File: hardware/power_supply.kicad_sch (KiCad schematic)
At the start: 24 parts, among them J4 POWER INPUT, U10 NCP1117-5.0, U11 LM2596DS-ADJ, U11 NCP1117-3.3

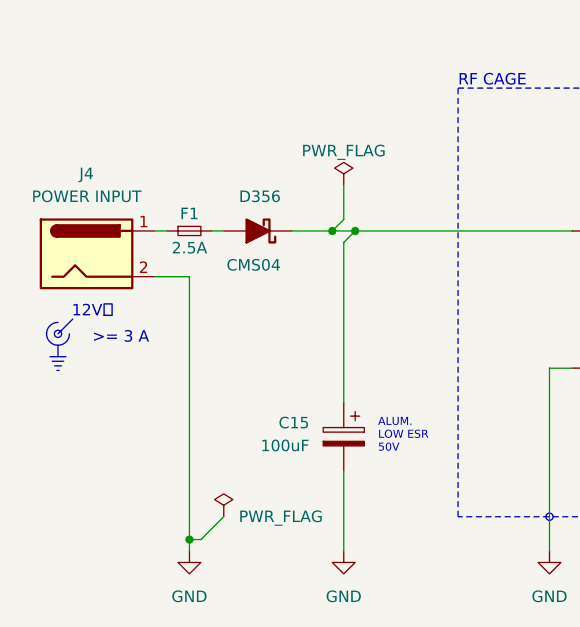
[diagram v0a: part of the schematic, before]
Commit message: Assign footprints
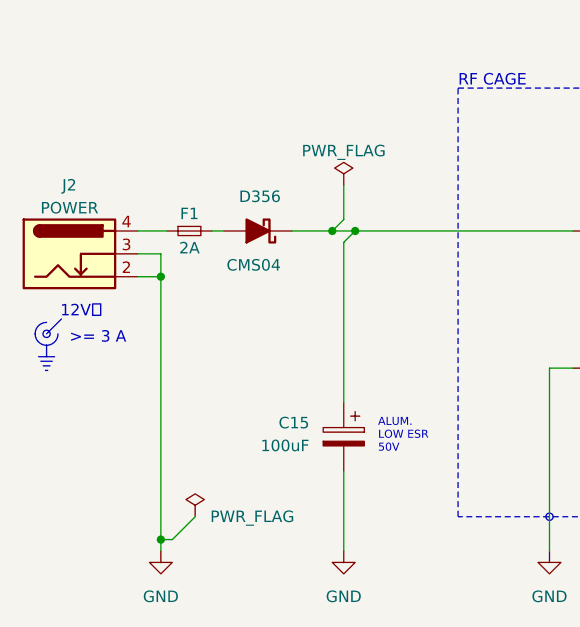
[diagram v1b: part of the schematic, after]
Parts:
- removed J4: POWER INPUT, symbol Connector:Jack-DC
- added J2: POWER, Connector_espena:DC-Power-Jack_DC044_5.5mm_2.1mm, symbol Connector_espena:Barrel_Jack_Switch
- C14, C19, C28: footprint (none) -> Capacitor_SMD_espena:CP_Elec_18x16.5
- C15: footprint (none) -> Capacitor_SMD:CP_Elec_8x10
- C16, C20, C21, C24, C26, C27, C31, C32: footprint (none) -> Capacitor_SMD:C_0805_2012Metric
- D355: footprint (none) -> Diode_SMD:D_SMA
- D356: footprint (none) -> Diode_SMD_mouser:SODFL4724X108N
- F1: value 2.5A -> 2A; footprint (none) -> Fuse_espena:FuseHolder_Keystone_3554
- L1: footprint (none) -> Inductor_SMD_espena:L_Pulse_LCI-44
- R20, R21: footprint (none) -> Resistor_SMD:R_0805_2012Metric
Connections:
- net GND: now also J2.2, J2.3
- net at F1.1: now also J2.4

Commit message: Starting PCB routing process
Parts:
- J2: footprint Connector_espena:DC-Power-Jack_DC044_5.5mm_2.1mm -> Connector_BarrelJack_espena:BarrelJack_DC044_Horizontal
- U11: footprint Package_TO_SOT_THT:TO-220-5_P3.4x3.7mm_StaggerOdd_Lead3.8mm_Vertical -> Regulator_SMD_mouser:NCP5663DSADJR4G
- renumbered U11 to U12, U11 to U13, U11 to U14
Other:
- moved on the sheet: D356, F1, R20, R21

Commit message: Routing in progress
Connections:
- net +3.3V_MCU: now reaches C31.1, U14.2 (VO)
- net +8.1V: now reaches C14.1, C16.2, C21.1, C24.1, C27.1, L1.2, R20.2, U10.3 (VI), U13.3 (VI), U14.3 (VI)
- net +3.3V_LED: now reaches C32.1, U13.2 (VO)
- net +3.3V_GPS: now reaches C26.1, C28.1, U12.2 (VO)
- net +5V: now reaches C19.1, C20.1, U10.2 (VO), U12.3 (VI)
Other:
- note removed: "5.0V"

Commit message: Prototype, starting on firmware
Former-commit-id: 3c22e4f94bda4a4eed472ac1ff762e7709731c05
Former-commit-id: afce4fecf5b4961621dea2f3a514203675ae8e80
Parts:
- added C25: 100uF, Capacitor_SMD:CP_Elec_8x10, symbol Device:C_Polarized
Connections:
- net +8.1V: now also C25.1
- net GND: now also C25.2
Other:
- moved on the sheet: C16, D355, L1, R20, R21, U11

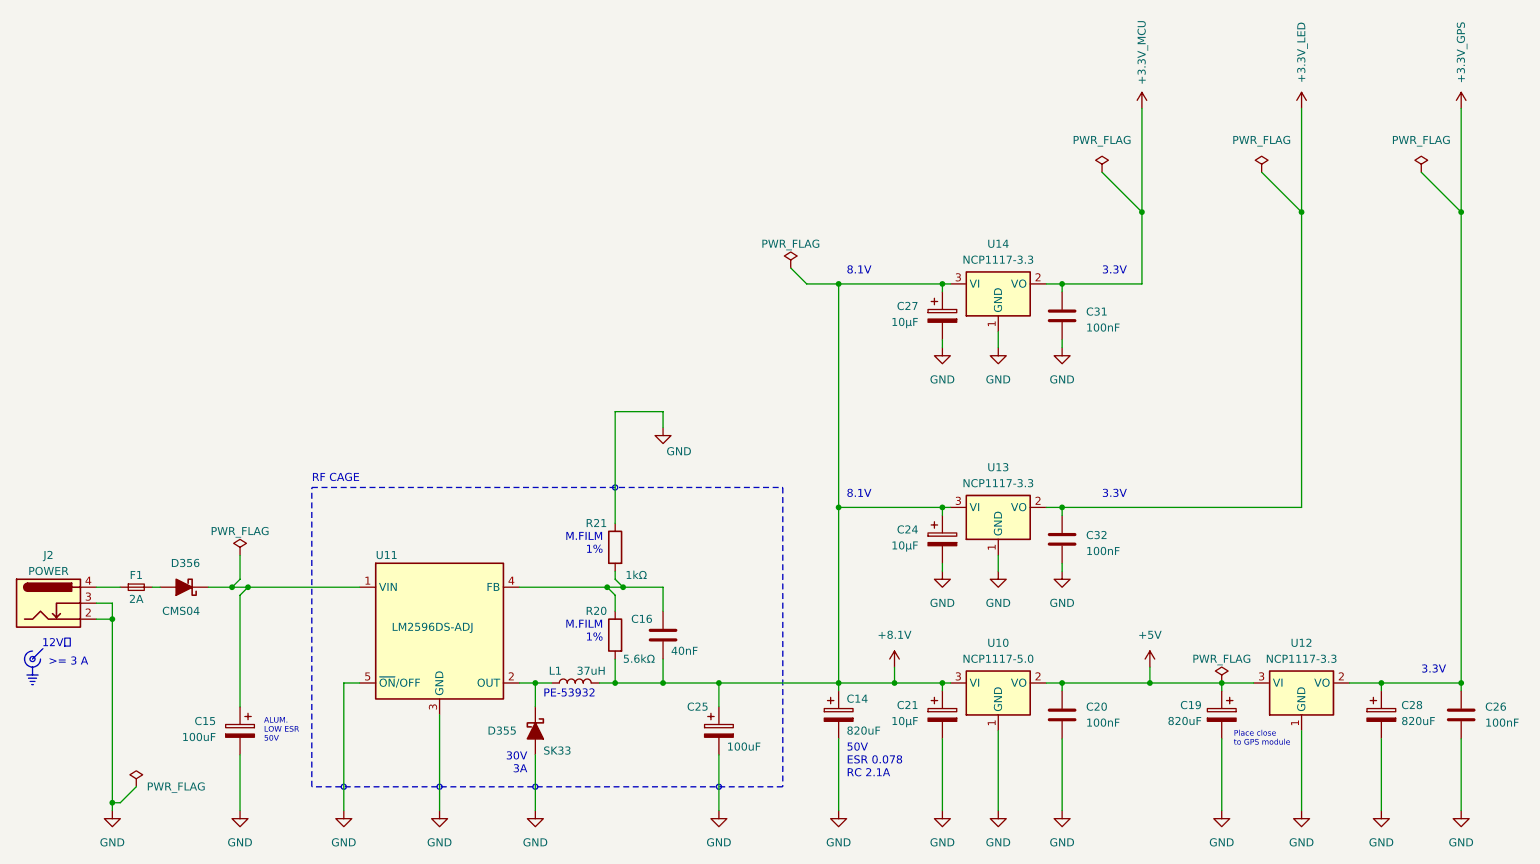
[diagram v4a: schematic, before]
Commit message: Change fuse from 2A to 250 mA
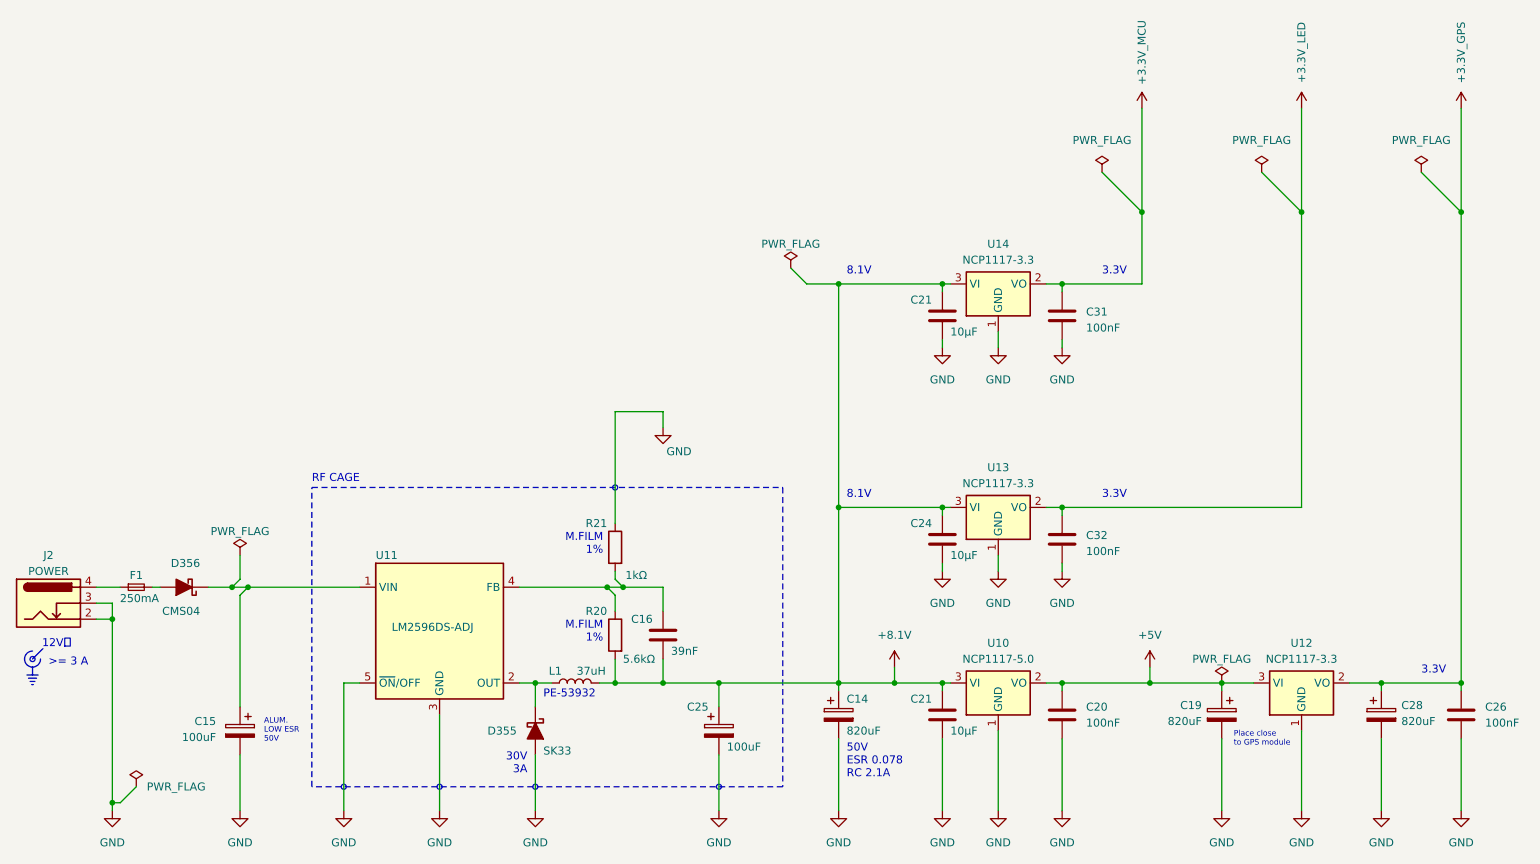
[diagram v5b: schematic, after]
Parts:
- removed C21, C24, C27: 10µF, Capacitor_SMD:C_0805_2012Metric, symbol Device:C_Polarized
- added C21 (x2), C24: 10µF, Capacitor_SMD:C_0805_2012Metric, symbol Device:C
- C16: value 40nF -> 39nF
- F1: value 2A -> 250mA
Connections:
- net +8.1V: now also C21.1, C21.1, C24.1
- net GND: now also C21.2, C21.2, C24.2
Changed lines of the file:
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@@
 	)
 	(symbol
-		(lib_id "Device:C_Polarized")
-		(at 176.53 132.08 0)
-		(unit 1)
-		(exclude_from_sim no)
-		(in_bom yes)
-		(on_board yes)
-		(dnp no)
-		(property "Reference" "C21"
-			(at 172.72 130.556 0)
-			(effects
-				(font
-					(size 1.27 1.27)
-				)
-				(justify right)
-			)
-		)
-		(property "Value" "10µF"
-			(at 172.72 133.096 0)
-			(effects
-				(font
-					(size 1.27 1.27)
-				)
-				(justify right)
-			)
-		)
-		(property "Footprint" "Capacitor_SMD:C_0805_2012Metric"
-			(at 177.4952 135.89 0)
-			(effects
-				(font
-					(size 1.27 1.27)
-				)
-				(hide yes)
-			)
-		)
-		(property "Datasheet" "~"
-			(at 176.53 132.08 0)
-			(effects
-				(font
-					(size 1.27 1.27)
-				)
-				(hide yes)
-			)
-		)
-		(property "Description" "Polarized capacitor"
-			(at 176.53 132.08 0)
-			(effects
-				(font
-					(size 1.27 1.27)
-				)
-				(hide yes)
-			)
-		)
-		(pin "1"
-		)
-		(pin "2"
-		)
-		(instances
-			(project "broadcast_clock"
-				(path "/40ecfd14-7e3d-4342-87f4-c464dfcd4cdf/08d14882-9adb-43c1-98ed-4244eb646c28"
-					(reference "C21")
-					(unit 1)
-				)
-			)
-		)
-	)
-	(symbol
 		(lib_id "Device:L")
 		(at 118.11 127 90)
@@
 	)
 	(symbol
-		(lib_id "Device:C_Polarized")
-		(at 176.53 68.58 0)
-		(unit 1)
-		(exclude_from_sim no)
-		(in_bom yes)
-		(on_board yes)
-		(dnp no)
-		(property "Reference" "C27"
-			(at 172.72 67.056 0)
-			(effects
-				(font
-					(size 1.27 1.27)
-				)
-				(justify right)
-			)
-		)
-		(property "Value" "10µF"
-			(at 172.72 69.596 0)
-			(effects
-				(font
-					(size 1.27 1.27)
-				)
-				(justify right)
-			)
-		)
-		(property "Footprint" "Capacitor_SMD:C_0805_2012Metric"
-			(at 177.4952 72.39 0)
-			(effects
-				(font
-					(size 1.27 1.27)
-				)
-				(hide yes)
-			)
-		)
-		(property "Datasheet" "~"
-			(at 176.53 68.58 0)
-			(effects
-				(font
-					(size 1.27 1.27)
-				)
-				(hide yes)
-			)
-		)
-		(property "Description" "Polarized capacitor"
-			(at 176.53 68.58 0)
-			(effects
-				(font
-					(size 1.27 1.27)
-				)
-				(hide yes)
-			)
-		)
-		(pin "1"
-		)
-		(pin "2"
-		)
-		(instances
-			(project "broadcast_clock"
-				(path "/40ecfd14-7e3d-4342-87f4-c464dfcd4cdf/08d14882-9adb-43c1-98ed-4244eb646c28"
-					(reference "C27")
-					(unit 1)
-				)
-			)
-		)
-	)
-	(symbol
 		(lib_id "power:GND")
 		(at 185.42 73.66 0)
@@
 	)
 	(symbol
+		(lib_id "Device:C")
+		(at 176.53 132.08 0)
+		(unit 1)
+		(exclude_from_sim no)
+		(in_bom yes)
+		(on_board yes)
+		(dnp no)
+		(property "Reference" "C21"
+			(at 171.45 129.54 0)
+			(effects
+				(font
+					(size 1.27 1.27)
+				)
+				(justify left)
+			)
+		)
+		(property "Value" "10µF"
+			(at 177.8 134.62 0)
+			(effects
+				(font
+					(size 1.27 1.27)
+				)
+				(justify left)
+			)
+		)
+		(property "Footprint" "Capacitor_SMD:C_0805_2012Metric"
+			(at 177.4952 135.89 0)
+			(effects
+				(font
+					(size 1.27 1.27)
+				)
+				(hide yes)
+			)
+		)
+		(property "Datasheet" "~"
+			(at 176.53 132.08 0)
+			(effects
+				(font
+					(size 1.27 1.27)
+				)
+				(hide yes)
+			)
+		)
+		(property "Description" "Unpolarized capacitor"
+			(at 176.53 132.08 0)
+			(effects
+				(font
+					(size 1.27 1.27)
+				)
+				(hide yes)
+			)
+		)
+		(pin "1"
+		)
+		(pin "2"
+		)
+		(instances
+			(project "broadcast_clock"
+				(path "/40ecfd14-7e3d-4342-87f4-c464dfcd4cdf/08d14882-9adb-43c1-98ed-4244eb646c28"
+					(reference "C21")
+					(unit 1)
+				)
+			)
+		)
+	)
+	(symbol
 		(lib_id "power_espena:+5V")
 		(at 209.55 124.46 0)
@@
 			)
 		)
-		(property "Value" "40nF"
+		(property "Value" "39nF"
 			(at 133.35 121.92 0)
 			(effects
@@
 			)
 		)
-		(property "Value" "2A"
-			(at 48.26 113.665 0)
+		(property "Value" "250mA"
+			(at 48.768 113.538 0)
 			(effects
 				(font
@@
 	(symbol
 		(lib_id "Device:C_Polarized")
-		(at 176.53 104.14 0)
-		(unit 1)
-		(exclude_from_sim no)
-		(in_bom yes)
-		(on_board yes)
-		(dnp no)
-		(property "Reference" "C24"
-			(at 172.72 102.616 0)
-			(effects
-				(font
-					(size 1.27 1.27)
-				)
-				(justify right)
-			)
-		)
-		(property "Value" "10µF"
-			(at 172.72 105.156 0)
-			(effects
-				(font
-					(size 1.27 1.27)
-				)
-				(justify right)
-			)
-		)
-		(property "Footprint" "Capacitor_SMD:C_0805_2012Metric"
-			(at 177.4952 107.95 0)
-			(effects
-				(font
-					(size 1.27 1.27)
-				)
-				(hide yes)
-			)
-		)
-		(property "Datasheet" "~"
-			(at 176.53 104.14 0)
-			(effects
-				(font
-					(size 1.27 1.27)
-				)
-				(hide yes)
-			)
-		)
-		(property "Description" "Polarized capacitor"
-			(at 176.53 104.14 0)
-			(effects
-				(font
-					(size 1.27 1.27)
-				)
-				(hide yes)
-			)
-		)
-		(pin "1"
-		)
-		(pin "2"
-		)
-		(instances
-			(project "broadcast_clock"
-				(path "/40ecfd14-7e3d-4342-87f4-c464dfcd4cdf/08d14882-9adb-43c1-98ed-4244eb646c28"
-					(reference "C24")
-					(unit 1)
-				)
-			)
-		)
-	)
-	(symbol
-		(lib_id "Device:C_Polarized")
 		(at 220.98 132.08 0)
 		(mirror y)
@@
 					(unit 1)
 				)
+			)
+		)
+	)
+	(symbol
+		(lib_id "Device:C")
+		(at 176.53 104.14 0)
+		(unit 1)
+		(exclude_from_sim no)
+		(in_bom yes)
+		(on_board yes)
+		(dnp no)
+		(property "Reference" "C24"
+			(at 171.45 101.6 0)
+			(effects
+				(font
+					(size 1.27 1.27)
+				)
+				(justify left)
+			)
+		)
+		(property "Value" "10µF"
+			(at 177.8 106.68 0)
+			(effects
+				(font
+					(size 1.27 1.27)
+				)
+				(justify left)
+			)
+		)
+		(property "Footprint" "Capacitor_SMD:C_0805_2012Metric"
+			(at 177.4952 107.95 0)
+			(effects
+				(font
+					(size 1.27 1.27)
+				)
+				(hide yes)
+			)
+		)
+		(property "Datasheet" "~"
+			(at 176.53 104.14 0)
+			(effects
+				(font
+					(size 1.27 1.27)
+				)
+				(hide yes)
+			)
+		)
+		(property "Description" "Unpolarized capacitor"
+			(at 176.53 104.14 0)
+			(effects
+				(font
+					(size 1.27 1.27)
+				)
+				(hide yes)
+			)
+		)
+		(pin "1"
+		)
+		(pin "2"
+		)
+		(instances
+			(project "broadcast_clock"
+				(path "/40ecfd14-7e3d-4342-87f4-c464dfcd4cdf/08d14882-9adb-43c1-98ed-4244eb646c28"
+					(reference "C24")
+					(unit 1)
+				)
+			)
+		)
+	)
+	(symbol
+		(lib_id "Device:C")
+		(at 176.53 68.58 0)
+		(unit 1)
+		(exclude_from_sim no)
+		(in_bom yes)
+		(on_board yes)
+		(dnp no)
+		(property "Reference" "C21"
+			(at 171.45 66.04 0)
+			(effects
+				(font
+					(size 1.27 1.27)
+				)
+				(justify left)
+			)
+		)
+		(property "Value" "10µF"
+			(at 177.8 71.12 0)
+			(effects
+				(font
+					(size 1.27 1.27)
+				)
+				(justify left)
+			)
+		)
+		(property "Footprint" "Capacitor_SMD:C_0805_2012Metric"
+			(at 177.4952 72.39 0)
+			(effects
+				(font
+					(size 1.27 1.27)
+				)
+				(hide yes)
+			)
+		)
+		(property "Datasheet" "~"
+			(at 176.53 68.58 0)
+			(effects
+				(font
+					(size 1.27 1.27)
+				)
+				(hide yes)
+			)
+		)
+		(property "Description" "Unpolarized capacitor"
+			(at 176.53 68.58 0)
+			(effects
+				(font
+					(size 1.27 1.27)
+				)
+				(hide yes)
+			)
+		)
+		(pin "1"
+		)
+		(pin "2"
+		)
+		(instances
+			(project "broadcast_clock"
+				(path "/40ecfd14-7e3d-4342-87f4-c464dfcd4cdf/08d14882-9adb-43c1-98ed-4244eb646c28"
+					(reference "C21")
+					(unit 1)
+				)

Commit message: Minor design updates
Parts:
- C14, C19, C28: value 820uF -> 820μF
- C15, C25: value 100uF -> 100μF
- R20: value 5.6kΩ -> 5,6kΩ
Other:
- note added: "VIA FENCE"
- note removed: "RF CAGE"
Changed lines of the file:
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@@
 		)
 	)
-	(text "RF CAGE"
+	(text "VIA FENCE"
 		(exclude_from_sim no)
 		(at 76.2 95.25 0)
@@
 			)
 		)
-		(property "Value" "100uF"
+		(property "Value" "100μF"
 			(at 142.24 137.16 0)
 			(effects
@@
 			)
 		)
-		(property "Value" "820uF"
+		(property "Value" "820μF"
 			(at 161.29 134.62 0)
 			(effects
@@
 			)
 		)
-		(property "Value" "820uF"
+		(property "Value" "820μF"
 			(at 249.555 133.096 0)
 			(effects
@@
 			)
 		)
-		(property "Value" "5.6kΩ"
+		(property "Value" "5,6kΩ"
 			(at 130.81 123.19 0)
 			(effects
@@
 			)
 		)
-		(property "Value" "100uF"
+		(property "Value" "100μF"
 			(at 60.96 135.636 0)
 			(effects
@@
 		(lib_id "Device:C_Polarized")
 		(at 220.98 132.08 0)
-		(mirror y)
 		(unit 1)
 		(exclude_from_sim no)
@@
 		(on_board yes)
 		(dnp no)
-		(fields_autoplaced yes)
 		(property "Reference" "C19"
-			(at 217.805 130.556 0)
+			(at 217.17 129.9209 0)
 			(effects
 				(font
 					(size 1.27 1.27)
 				)
-				(justify left)
+				(justify right)
 			)
 		)
-		(property "Value" "820uF"
-			(at 217.805 133.096 0)
+		(property "Value" "820μF"
+			(at 217.17 132.4609 0)
 			(effects
 				(font
 					(size 1.27 1.27)
 				)
-				(justify left)
+				(justify right)
 			)
 		)
 		(property "Footprint" "Capacitor_SMD_espena:CP_Elec_18x16.5"
-			(at 220.0148 135.89 0)
+			(at 221.9452 135.89 0)
 			(effects
 				(font

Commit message: Prepare v8 project for KiCAD version 9
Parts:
- renumbered C21 to C27
